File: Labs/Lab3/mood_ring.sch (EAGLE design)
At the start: 7 parts

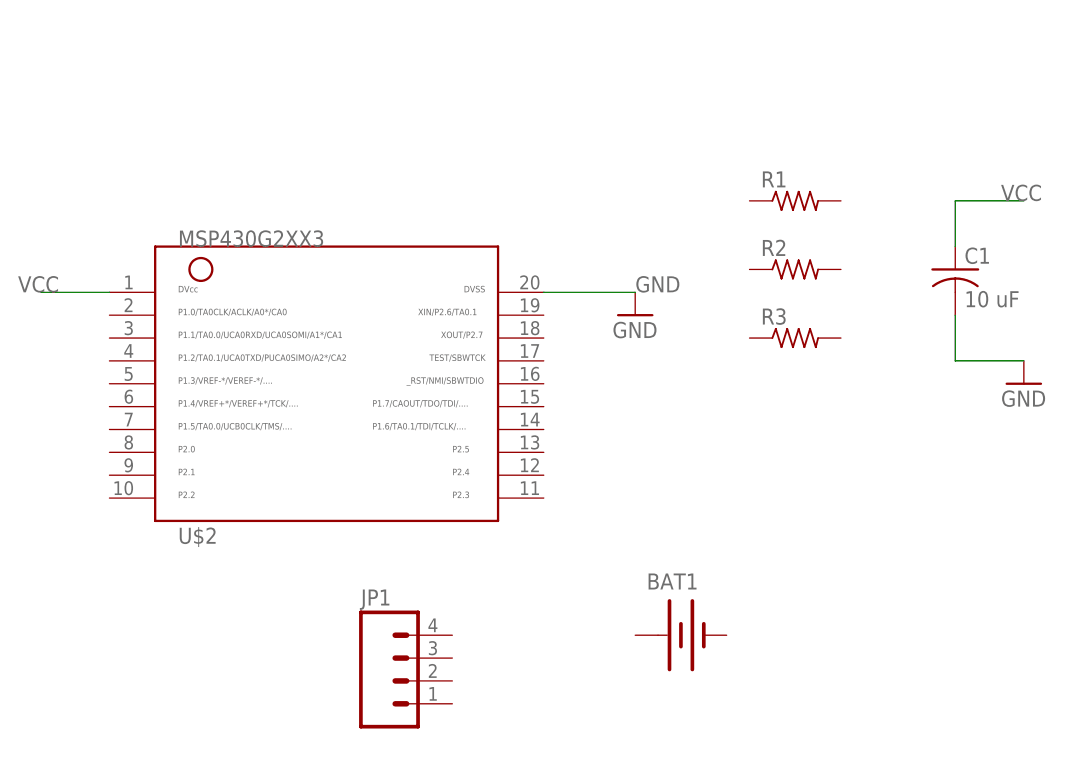
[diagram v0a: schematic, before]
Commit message: Added resistor for reset pin
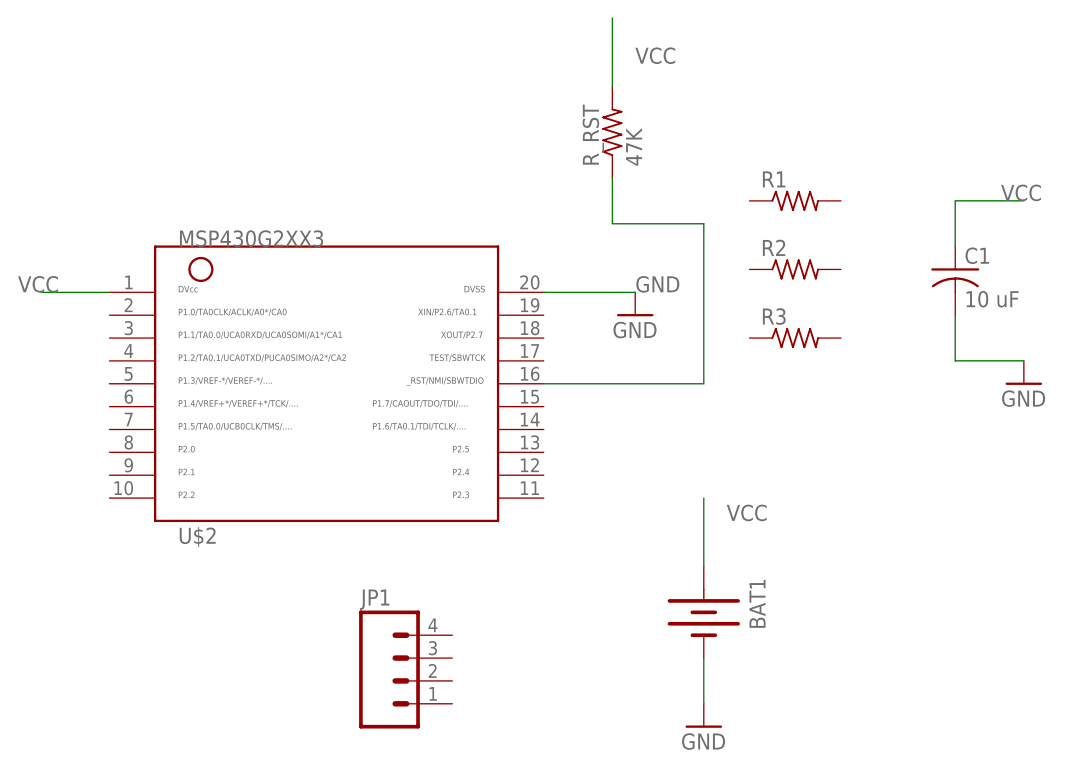
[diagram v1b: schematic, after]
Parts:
- added R_RST: 47K, resistor:R-US_R1206
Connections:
- new net N$1: R_RST.1, U$2.16
- net GND: now also BAT1.-
- net VCC: now also BAT1.+, R_RST.2
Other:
- moved on the sheet: BAT1
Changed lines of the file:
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@@
 <?xml version="1.0" encoding="utf-8"?>
 <!DOCTYPE eagle SYSTEM "eagle.dtd">
-<eagle version="7.3.0">
+<eagle version="8.6.0">
 <drawing>
 <settings>
 <setting alwaysvectorfont="no"/>
+<setting keepoldvectorfont="yes"/>
 <setting verticaltext="up"/>
 </settings>
@@
 <part name="GND1" library="supply1" deviceset="GND" device=""/>
 <part name="GND2" library="supply1" deviceset="GND" device=""/>
+<part name="GND3" library="supply1" deviceset="GND" device=""/>
+<part name="R_RST" library="resistor" deviceset="R-US_" device="R1206" value="47K"/>
 </parts>
 <sheets>
@@
 <instance part="R2" gate="G$1" x="27.94" y="182.88"/>
 <instance part="R3" gate="G$1" x="27.94" y="175.26"/>
-<instance part="BAT1" gate="G$1" x="15.24" y="142.24"/>
+<instance part="BAT1" gate="G$1" x="17.78" y="144.78" rot="R270"/>
 <instance part="C1" gate="G$1" x="45.72" y="182.88"/>
 <instance part="GND1" gate="1" x="10.16" y="177.8"/>
 <instance part="GND2" gate="1" x="53.34" y="170.18"/>
+<instance part="GND3" gate="1" x="17.78" y="132.08"/>
+<instance part="R_RST" gate="G$1" x="7.62" y="198.12" rot="R90"/>
 </instances>
 <busses>
@@
 <label x="50.8" y="190.5" size="1.778" layer="95"/>
 </segment>
+<segment>
+<pinref part="BAT1" gate="G$1" pin="+"/>
+<wire x1="17.78" y1="149.86" x2="17.78" y2="157.48" width="0.1524" layer="91"/>
+<label x="20.32" y="154.94" size="1.778" layer="95"/>
+</segment>
+<segment>
+<pinref part="R_RST" gate="G$1" pin="2"/>
+<wire x1="7.62" y1="203.2" x2="7.62" y2="210.82" width="0.1524" layer="91"/>
+<label x="10.16" y="205.74" size="1.778" layer="95"/>
+</segment>
 </net>
 <net name="GND" class="0">
@@
 <pinref part="GND2" gate="1" pin="GND"/>
 </segment>
+<segment>
+<pinref part="BAT1" gate="G$1" pin="-"/>
+<wire x1="17.78" y1="139.7" x2="17.78" y2="134.62" width="0.1524" layer="91"/>
+<pinref part="GND3" gate="1" pin="GND"/>
+</segment>
 </net>
+<net name="N$1" class="0">
+<segment>
+<pinref part="U$2" gate="G$1" pin="16"/>
+<wire x1="0" y1="170.18" x2="17.78" y2="170.18" width="0.1524" layer="91"/>
+<wire x1="17.78" y1="170.18" x2="17.78" y2="187.96" width="0.1524" layer="91"/>
+<wire x1="17.78" y1="187.96" x2="7.62" y2="187.96" width="0.1524" layer="91"/>
+<wire x1="7.62" y1="187.96" x2="7.62" y2="193.04" width="0.1524" layer="91"/>
+<pinref part="R_RST" gate="G$1" pin="1"/>
+</segment>
+</net>
